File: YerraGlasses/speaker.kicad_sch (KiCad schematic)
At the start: 6 parts, among them U2 MAX98357A, U3 MAX98357A

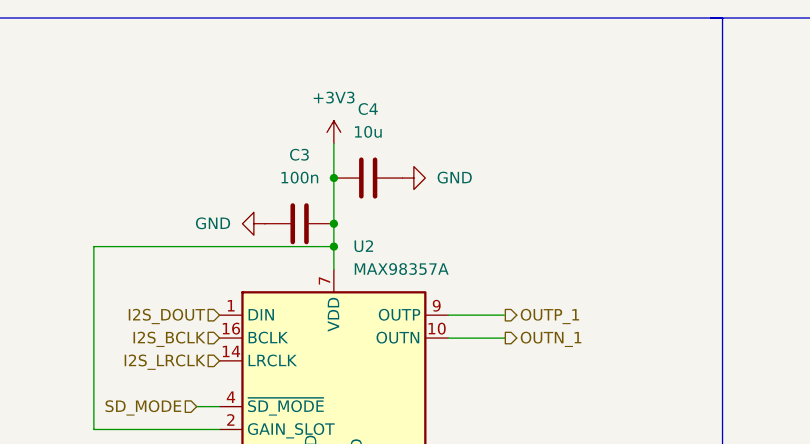
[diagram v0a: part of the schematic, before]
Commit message: added power connector, updated cad
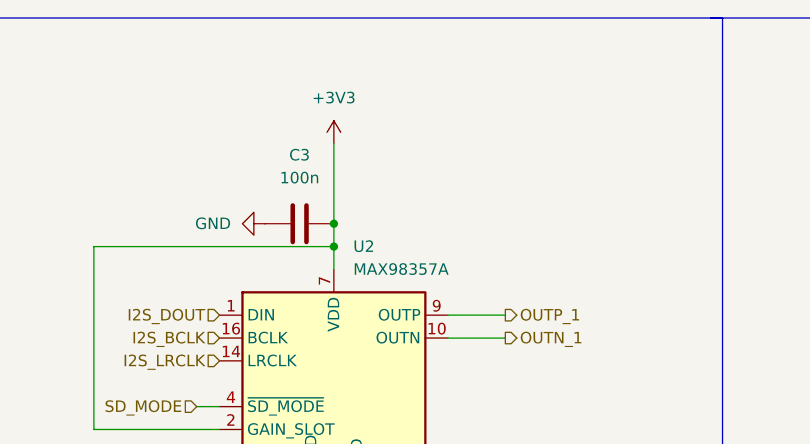
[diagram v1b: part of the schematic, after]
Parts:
- removed C4: 10u, Capacitor_SMD:C_0805_2012Metric, symbol Device:C
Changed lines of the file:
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@@
-	)
-	(junction
-		(at 60.96 36.83)
-		(diameter 0)
-		(color 0 0 0 0)
 	)
 	(junction
@@
 	(wire
 		(pts
-			(xy 60.96 33.02) (xy 60.96 36.83)
+			(xy 60.96 33.02) (xy 60.96 41.91)
 		)
 		(stroke
@@
 		(pts
 			(xy 102.87 19.05) (xy 104.14 19.05)
-		)
-		(stroke
-			(width 0)
-			(type default)
-		)
-	)
-	(wire
-		(pts
-			(xy 60.96 36.83) (xy 60.96 41.91)
 		)
 		(stroke
@@
 	(symbol
 		(lib_id "power:GND")
-		(at 68.58 36.83 90)
-		(unit 1)
-		(exclude_from_sim no)
-		(in_bom yes)
-		(on_board yes)
-		(dnp no)
-		(fields_autoplaced yes)
-		(property "Reference" "#PWR09"
-			(at 74.93 36.83 0)
-			(effects
-				(font
-					(size 1.27 1.27)
-				)
-				(hide yes)
-			)
-		)
-		(property "Value" "GND"
-			(at 72.39 36.8299 90)
-			(effects
-				(font
-					(size 1.27 1.27)
-				)
-				(justify right)
-			)
-		)
-		(property "Footprint" ""
-			(at 68.58 36.83 0)
-			(effects
-				(font
-					(size 1.27 1.27)
-				)
-				(hide yes)
-			)
-		)
-		(property "Datasheet" ""
-			(at 68.58 36.83 0)
-			(effects
-				(font
-					(size 1.27 1.27)
-				)
-				(hide yes)
-			)
-		)
-		(property "Description" "Power symbol creates a global label with name \"GND\" , ground"
-			(at 68.58 36.83 0)
-			(effects
-				(font
-					(size 1.27 1.27)
-				)
-				(hide yes)
-			)
-		)
-		(pin "1"
-		)
-		(instances
-			(project "Hansoglasses"
-				(path "/565dd4cd-3458-4e26-8cb8-cc6b370af252/b2b51a2c-670d-4f2e-9a6b-3b326a8374fa"
-					(reference "#PWR09")
-					(unit 1)
-				)
-			)
-		)
-	)
-	(symbol
-		(lib_id "power:GND")
 		(at 157.48 33.02 90)
 		(unit 1)
@@
 					(unit 1)
 				)
-			)
-		)
-	)
-	(symbol
-		(lib_id "Device:C")
-		(at 64.77 36.83 270)
-		(unit 1)
-		(exclude_from_sim no)
-		(in_bom yes)
-		(on_board yes)
-		(dnp no)
-		(fields_autoplaced yes)
-		(property "Reference" "C4"
-			(at 64.77 29.21 90)
-			(effects
-				(font
-					(size 1.27 1.27)
-				)
-			)
-		)
-		(property "Value" "10u"
-			(at 64.77 31.75 90)
-			(effects
-				(font
-					(size 1.27 1.27)
-				)
-			)
-		)
-		(property "Footprint" "Capacitor_SMD:C_0805_2012Metric"
-			(at 60.96 37.7952 0)
-			(effects
-				(font
-					(size 1.27 1.27)
-				)
-				(hide yes)
-			)
-		)
-		(property "Datasheet" "https://www.mouser.com/datasheet/3/76/1/GRM21BR61H106KE43_01A.pdf"
-			(at 64.77 36.83 0)
-			(effects
-				(font
-					(size 1.27 1.27)
-				)
-				(hide yes)
-			)
-		)
-		(property "Description" "Unpolarized capacitor"
-			(at 64.77 36.83 0)
-			(effects
-				(font
-					(size 1.27 1.27)
-				)
-				(hide yes)
-			)
-		)
-		(property "Mouser #" "81-GRM21BR61H106KE3L"
-			(at 64.77 36.83 0)
-			(effects
-				(font
-					(size 1.27 1.27)
-				)
-				(hide yes)
-			)
-		)
-		(property "Mouser Link" "https://www.mouser.com/ProductDetail/Murata-Electronics/GRM21BR61H106KE43L?qs=lYGu3FyN48cBZlIduWKclg%3D%3D&srsltid=AfmBOoovanZHDCILOsTNmRDlbeowyCnSNVD-tyLdgO5iJbYQ29cv4-uh"
-			(at 64.77 36.83 0)
-			(effects
-				(font
-					(size 1.27 1.27)
-				)
-				(hide yes)
-			)
-		)
-		(property "JLCPCB #" "C440198"
-			(at 64.77 36.83 0)
-			(effects
-				(font
-					(size 1.27 1.27)
-				)
-				(hide yes)
-			)
-		)
-		(property "Mouser Part Number" "81-GRM21BR61H106KE3L"
-			(at 64.77 36.83 0)
-			(effects
-				(font
-					(size 1.27 1.27)
-				)
-				(hide yes)
-			)
-		)
-		(pin "2"
-		)
-		(pin "1"
-		)
-		(instances
-			(project "Hansoglasses"
-				(path "/565dd4cd-3458-4e26-8cb8-cc6b370af252/b2b51a2c-670d-4f2e-9a6b-3b326a8374fa"
-					(reference "C4")
-					(unit 1)
-				)
